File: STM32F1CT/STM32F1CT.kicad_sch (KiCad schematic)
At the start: 9 parts, among them U1 STM32F103C8T6

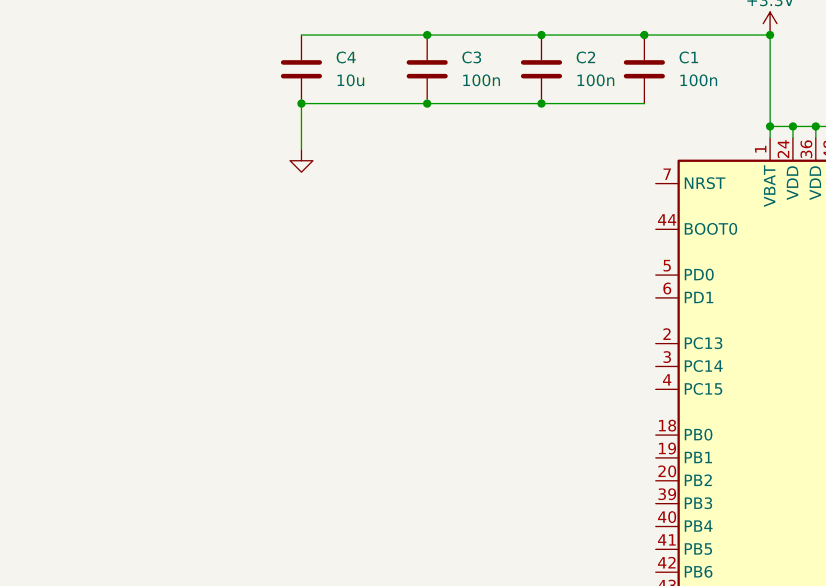
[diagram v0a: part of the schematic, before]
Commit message: BOOT and Reset
Edited boot and reset pins
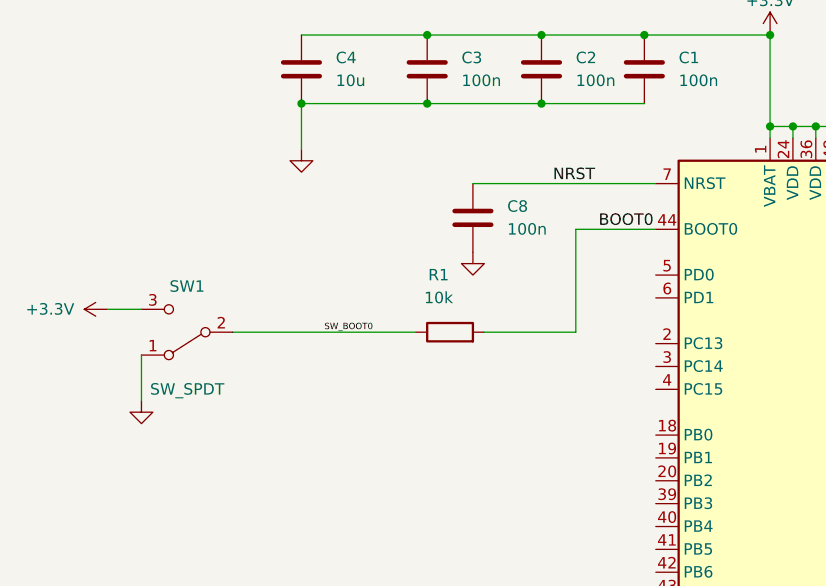
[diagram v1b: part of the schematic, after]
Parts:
- added C8: 100n, symbol Device:C
- added R1: 10k, symbol Device:R
- added SW1: SW_SPDT, symbol Switch:SW_SPDT
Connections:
- net +3.3V: now also SW1.3 (C)
- net GND: now also C8.2, SW1.1 (A)
- net BOOT0: now reaches U1.44 (BOOT0)
- net BOOT0: now also R1.2
- net NRST: now reaches U1.7 (NRST)
- net NRST: now also C8.1
- new net SW_BOOT0: R1.1, SW1.2 (B)
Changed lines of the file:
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@@
+    (stroke (width 0) (type default))
+  )
+  (wire (pts (xy 46.99 83.82) (xy 46.99 88.9))
     (stroke (width 0) (type default))
   )
@@
     (stroke (width 0) (type default))
   )
+  (wire (pts (xy 83.82 64.77) (xy 104.14 64.77))
+    (stroke (width 0) (type default))
+  )
   (wire (pts (xy 116.84 58.42) (xy 116.84 59.69))
     (stroke (width 0) (type default))
@@
     (stroke (width 0) (type default))
   )
+  (wire (pts (xy 57.15 81.28) (xy 77.47 81.28))
+    (stroke (width 0) (type default))
+  )
   (wire (pts (xy 78.74 48.26) (xy 91.44 48.26))
     (stroke (width 0) (type default))
@@
     (stroke (width 0) (type default))
   )
+  (wire (pts (xy 43.18 78.74) (xy 46.99 78.74))
+    (stroke (width 0) (type default))
+  )
   (wire (pts (xy 119.38 140.97) (xy 121.92 140.97))
     (stroke (width 0) (type default))
   )
+  (wire (pts (xy 95.25 81.28) (xy 95.25 69.85))
+    (stroke (width 0) (type default))
+  )
   (wire (pts (xy 91.44 48.26) (xy 102.87 48.26))
     (stroke (width 0) (type default))
   )
+  (wire (pts (xy 95.25 69.85) (xy 104.14 69.85))
+    (stroke (width 0) (type default))
+  )
   (wire (pts (xy 127 59.69) (xy 127 44.45))
     (stroke (width 0) (type default))
@@
     (stroke (width 0) (type default))
   )
+  (wire (pts (xy 85.09 81.28) (xy 95.25 81.28))
+    (stroke (width 0) (type default))
+  )
   (wire (pts (xy 147.32 44.45) (xy 162.56 44.45))
     (stroke (width 0) (type default))
@@
     (stroke (width 0) (type default))
   )
+  (label "SW_BOOT0" (at 67.31 81.28 0) (fields_autoplaced)
+    (effects (font (size 0.7 0.7)) (justify left bottom))
+  )
+  (label "BOOT0" (at 97.79 69.85 0) (fields_autoplaced)
+    (effects (font (size 1.27 1.27)) (justify left bottom))
+  )
+  (label "NRST" (at 92.71 64.77 0) (fields_autoplaced)
+    (effects (font (size 1.27 1.27)) (justify left bottom))
+  )
   (symbol (lib_id "Device:C") (at 162.56 48.26 0) (unit 1)
     (in_bom yes) (on_board yes) (dnp no)
@@
     )
   )
+  (symbol (lib_id "Device:R") (at 81.28 81.28 90) (unit 1)
+    (in_bom yes) (on_board yes) (dnp no)
+    (property "Reference" "R1" (at 80.01 74.93 90)
+      (effects (font (size 1.27 1.27)))
+    )
+    (property "Value" "10k" (at 80.01 77.47 90)
+      (effects (font (size 1.27 1.27)))
+    )
+    (property "Footprint" "" (at 81.28 83.058 90)
+      (effects (font (size 1.27 1.27)) hide)
+    )
+    (property "Datasheet" "~" (at 81.28 81.28 0)
+      (effects (font (size 1.27 1.27)) hide)
+    )
+    (pin "2")
+    (pin "1")
+    (instances
+      (project "STM32F1CT"
+        (path "/f0aa6fd5-1695-4f55-ae2e-e69da917b85d"
+          (reference "R1") (unit 1)
+        )
+      )
+    )
+  )
   (symbol (lib_id "power:GND") (at 189.23 55.88 0) (unit 1)
     (in_bom yes) (on_board yes) (dnp no) (fields_autoplaced)
@@
     )
   )
+  (symbol (lib_id "Switch:SW_SPDT") (at 52.07 81.28 180) (unit 1)
+    (in_bom yes) (on_board yes) (dnp no)
+    (property "Reference" "SW1" (at 52.07 76.2 0)
+      (effects (font (size 1.27 1.27)))
+    )
+    (property "Value" "SW_SPDT" (at 52.07 87.63 0)
+      (effects (font (size 1.27 1.27)))
+    )
+    (property "Footprint" "" (at 52.07 81.28 0)
+      (effects (font (size 1.27 1.27)) hide)
+    )
+    (property "Datasheet" "~" (at 52.07 81.28 0)
+      (effects (font (size 1.27 1.27)) hide)
+    )
+    (pin "1")
+    (pin "3")
+    (pin "2")
+    (instances
+      (project "STM32F1CT"
+        (path "/f0aa6fd5-1695-4f55-ae2e-e69da917b85d"
+          (reference "SW1") (unit 1)
+        )
+      )
+    )
+  )
+  (symbol (lib_id "power:+3.3V") (at 43.18 78.74 90) (unit 1)
+    (in_bom yes) (on_board yes) (dnp no)
+    (property "Reference" "#PWR010" (at 46.99 78.74 0)
+      (effects (font (size 1.27 1.27)) hide)
+    )
+    (property "Value" "+3.3V" (at 36.83 78.74 90)
+      (effects (font (size 1.27 1.27)))
+    )
+    (property "Footprint" "" (at 43.18 78.74 0)
+      (effects (font (size 1.27 1.27)) hide)
+    )
+    (property "Datasheet" "" (at 43.18 78.74 0)
+      (effects (font (size 1.27 1.27)) hide)
+    )
+    (pin "1")
+    (instances
+      (project "STM32F1CT"
+        (path "/f0aa6fd5-1695-4f55-ae2e-e69da917b85d"
+          (reference "#PWR010") (unit 1)
+        )
+      )
+    )
+  )
   (symbol (lib_id "power:GND") (at 162.56 54.61 0) (unit 1)
     (in_bom yes) (on_board yes) (dnp no) (fields_autoplaced)
@@
         (path "/f0aa6fd5-1695-4f55-ae2e-e69da917b85d"
           (reference "#PWR05") (unit 1)
+        )
+      )
+    )
+  )
+  (symbol (lib_id "power:GND") (at 46.99 88.9 0) (unit 1)
+    (in_bom yes) (on_board yes) (dnp no) (fields_autoplaced)
+    (property "Reference" "#PWR09" (at 46.99 95.25 0)
+      (effects (font (size 1.27 1.27)) hide)
+    )
+    (property "Value" "GND" (at 46.99 93.98 0)
+      (effects (font (size 1.27 1.27)) hide)
+    )
+    (property "Footprint" "" (at 46.99 88.9 0)
+      (effects (font (size 1.27 1.27)) hide)
+    )
+    (property "Datasheet" "" (at 46.99 88.9 0)
+      (effects (font (size 1.27 1.27)) hide)
+    )
+    (pin "1")
+    (instances
+      (project "STM32F1CT"
+        (path "/f0aa6fd5-1695-4f55-ae2e-e69da917b85d"
+          (reference "#PWR09") (unit 1)
         )
       )
@@
     )
   )
+  (symbol (lib_id "Device:C") (at 83.82 68.58 0) (unit 1)
+    (in_bom yes) (on_board yes) (dnp no)
+    (property "Reference" "C8" (at 87.63 67.31 0)
+      (effects (font (size 1.27 1.27)) (justify left))
+    )
+    (property "Value" "100n" (at 87.63 69.85 0)
+      (effects (font (size 1.27 1.27)) (justify left))
+    )
+    (property "Footprint" "" (at 84.7852 72.39 0)
+      (effects (font (size 1.27 1.27)) hide)
+    )
+    (property "Datasheet" "~" (at 83.82 68.58 0)
+      (effects (font (size 1.27 1.27)) hide)
+    )
+    (pin "1")
+    (pin "2")
+    (instances
+      (project "STM32F1CT"
+        (path "/f0aa6fd5-1695-4f55-ae2e-e69da917b85d"
+          (reference "C8") (unit 1)
+        )
+      )
+    )
+  )
   (symbol (lib_id "power:+3.3VA") (at 127 44.45 0) (unit 1)
     (in_bom yes) (on_board yes) (dnp no) (fields_autoplaced)
@@
         )
       )
+    )
+  )
+  (symbol (lib_id "power:GND") (at 83.82 72.39 0) (unit 1)
+    (in_bom yes) (on_board yes) (dnp no) (fields_autoplaced)
+    (property "Reference" "#PWR08" (at 83.82 78.74 0)
+      (effects (font (size 1.27 1.27)) hide)
+    )
+    (property "Value" "GND" (at 83.82 77.47 0)
+      (effects (font (size 1.27 1.27)) hide)
+    )
+    (property "Footprint" "" (at 83.82 72.39 0)
+      (effects (font (size 1.27 1.27)) hide)
+    )
+    (property "Datasheet" "" (at 83.82 72.39 0)
+      (effects (font (size 1.27 1.27)) hide)
+    )
+    (pin "1")
+    (instances
+      (project "STM32F1CT"
+        (path "/f0aa6fd5-1695-4f55-ae2e-e69da917b85d"
+          (reference "#PWR08") (unit 1)
+        )
+      )
